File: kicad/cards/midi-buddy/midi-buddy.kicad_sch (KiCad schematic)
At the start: 20 parts, among them J1 Conn_01x06_Pin, J2 Conn_01x06_Pin, J4 Conn_01x05, U1 THVD1450DR, U2 STM32C011F4Px

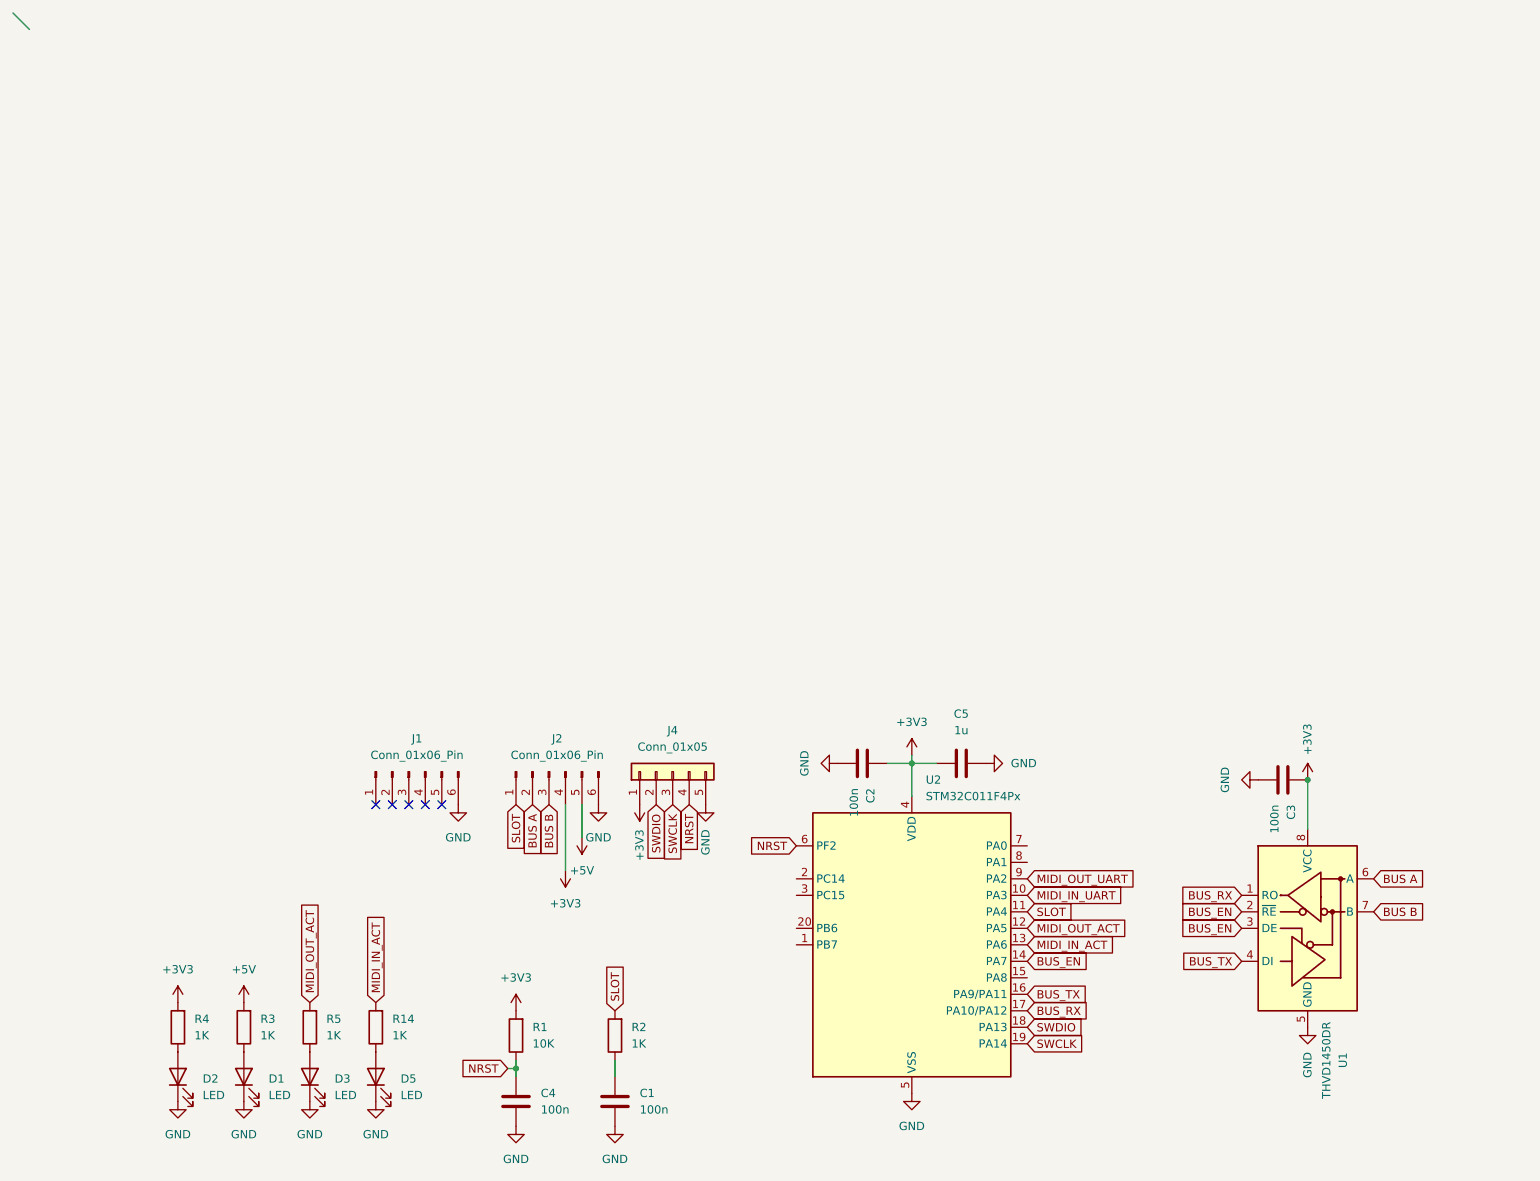
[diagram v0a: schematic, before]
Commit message: Update card template and MIDI Buddy
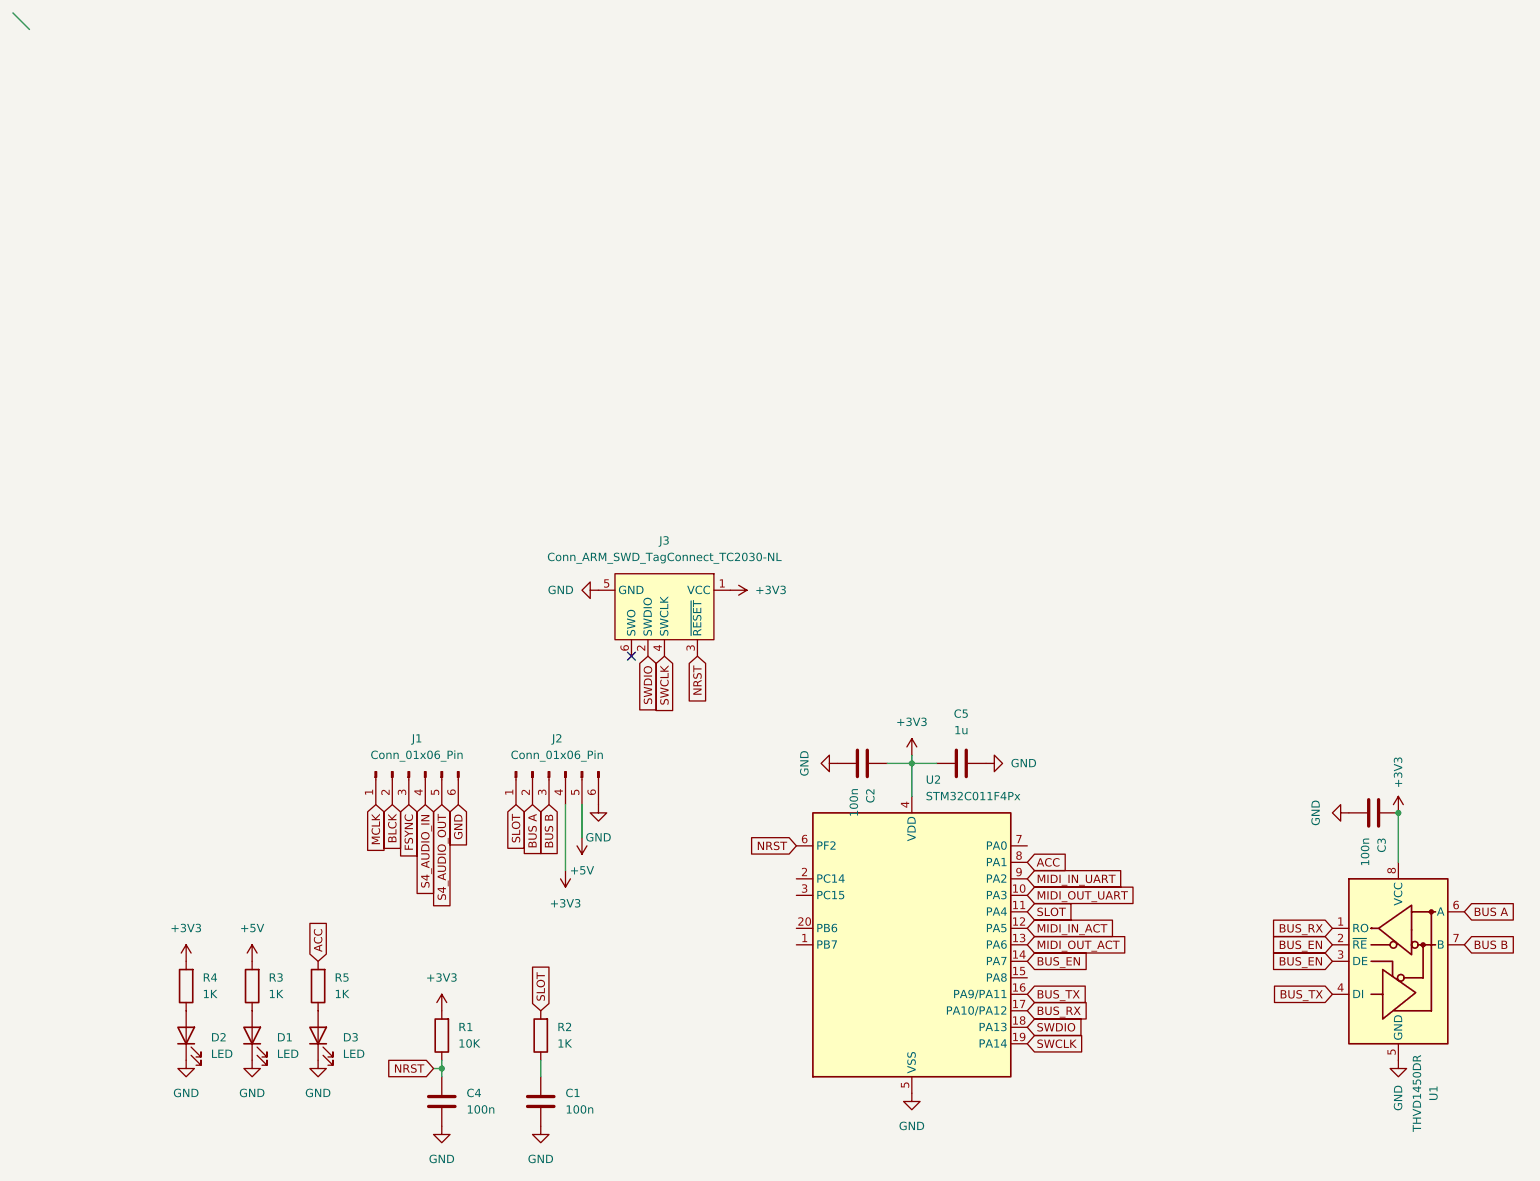
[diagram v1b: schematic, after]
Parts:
- removed D5: LED, LED_SMD:LED_1206_3216Metric, symbol Device:LED
- removed J4: Conn_01x05, Connector_PinHeader_1.27mm:PinHeader_1x05_P1.27mm_Vertical, symbol Connector_Generic:Conn_01x05
- removed R14: 1K, Resistor_SMD:R_0603_1608Metric, symbol Device:R
- added J3: Conn_ARM_SWD_TagConnect_TC2030-NL, Connector:Tag-Connect_TC2030-IDC-NL_2x03_P1.27mm_Vertical, symbol Connector:Conn_ARM_SWD_TagConnect_TC2030-NL
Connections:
- net +3V3: now also J3.1 (VCC)
- net GND: now also J3.5 (GND)
- net MIDI_IN_ACT: now also U2.12 (PA5); no longer U2.13 (PA6)
- net MIDI_IN_UART: now also U2.9 (PA2); no longer U2.10 (PA3)
- net MIDI_OUT_ACT: now also U2.13 (PA6); no longer R5.2, U2.12 (PA5)
- net MIDI_OUT_UART: now also U2.10 (PA3); no longer U2.9 (PA2)
- net NRST: now also J3.3 (~{RESET})
- net SWCLK: now also J3.4 (SWCLK)
- net SWDIO: now also J3.2 (SWDIO)
- net MCLK: now reaches J1.1 (Pin_1)
- net BLCK: now reaches J1.2 (Pin_2)
- net FSYNC: now reaches J1.3 (Pin_3)
- net S4_AUDIO_IN: now reaches J1.4 (Pin_4)
- net S4_AUDIO_OUT: now reaches J1.5 (Pin_5)
- net ACC: now reaches U2.8 (PA1)
- net ACC: now also R5.2
- no-connect marks 5 -> 1
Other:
- moved on the sheet: C1, C3, C4, D1, D2, D3, R1, R2, R3, R4, R5, U1
